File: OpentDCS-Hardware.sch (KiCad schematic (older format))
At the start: 4 parts

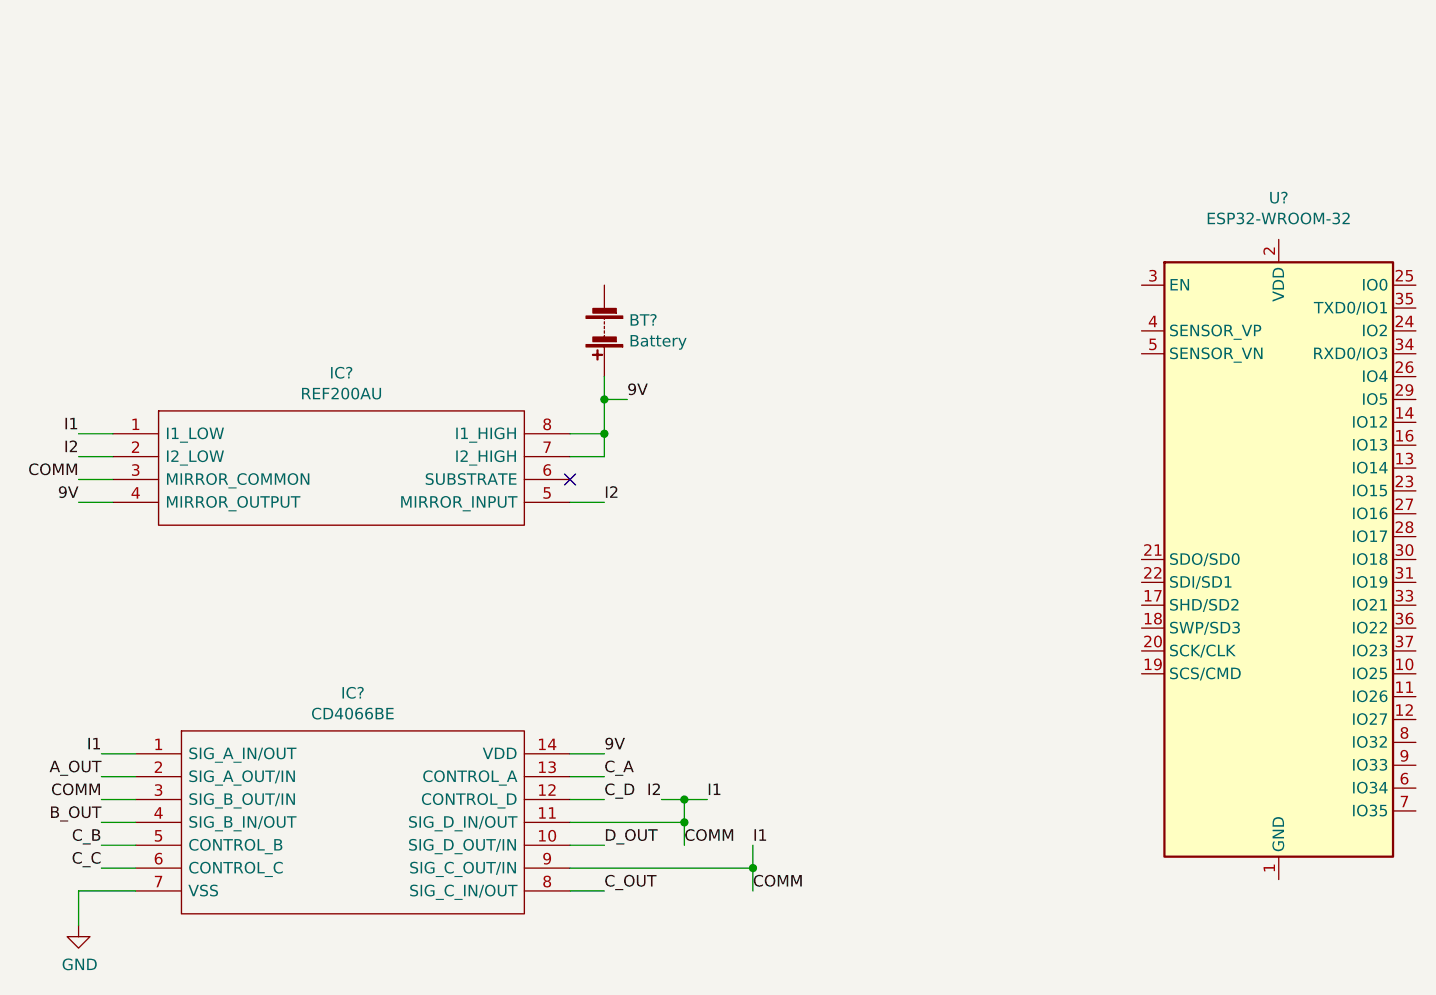
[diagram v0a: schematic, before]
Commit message: Combinações de corrente para o REF200
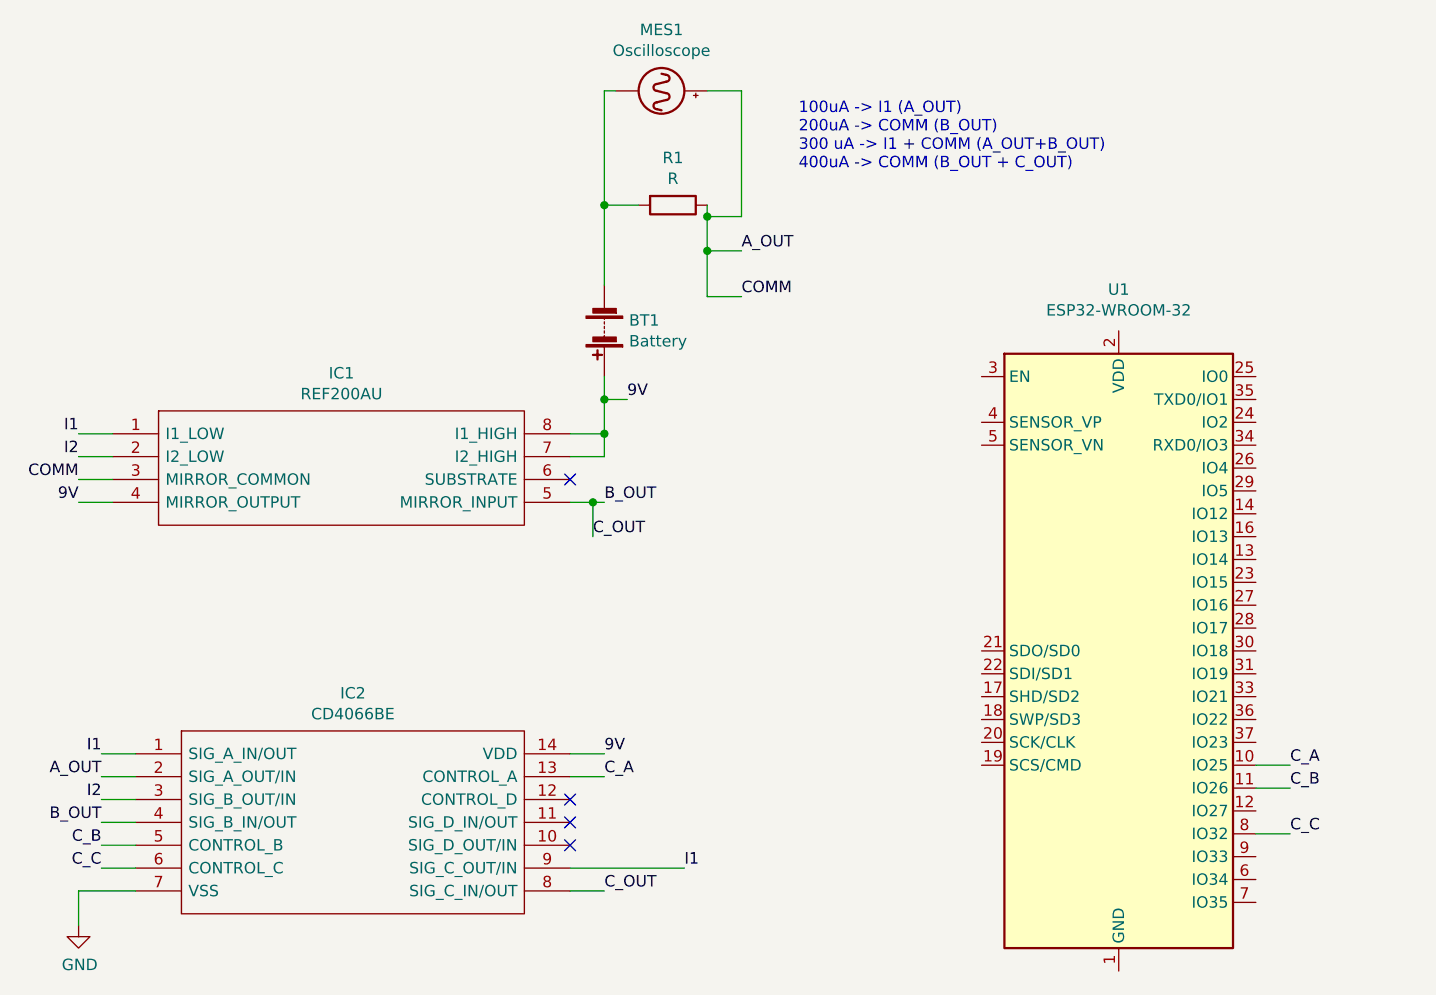
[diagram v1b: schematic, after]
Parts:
- added MES1: Oscilloscope, symbol Device:Oscilloscope
- added R1: R, symbol Device:R
- gave numbers to parts that had none: 4
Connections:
- net C_OUT is gone; now on net B_OUT: IC2.8 (SIG_C_IN/OUT)
- net A_OUT: now also IC1.3 (MIRROR_COMMON), MES1.2 (+), R1.1
- net B_OUT: now also IC1.5 (MIRROR_INPUT)
- net C_A: now also U1.10 (IO25)
- net C_B: now also U1.11 (IO26)
- net C_C: now also U1.8 (IO32)
- net at BT1.2 (-): now also MES1.1 (-), R1.2
- removed net COMM: IC1.1 (I1_LOW), IC1.2 (I2_LOW), IC1.3 (MIRROR_COMMON), IC1.5 (MIRROR_INPUT), IC2.1 (SIG_A_IN/OUT), IC2.11 (SIG_D_IN/OUT), IC2.3 (SIG_B_OUT/IN), IC2.9 (SIG_C_OUT/IN)
- net C_D: no longer names the net of IC2.12 (CONTROL_D)
- net D_OUT: no longer names the net of IC2.10 (SIG_D_OUT/IN)
- new net I1: IC1.1 (I1_LOW), IC2.1 (SIG_A_IN/OUT), IC2.9 (SIG_C_OUT/IN)
- new net I2: IC1.2 (I2_LOW), IC2.3 (SIG_B_OUT/IN)
- no-connect marks 1 -> 4
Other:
- note added: "100uA -> I1 (A_OUT)\n200uA -> COMM (B_OUT)\n300 uA -> I1 + COMM (A_OUT+B_OUT)\n400uA -> COMM (B_OUT + C_OUT)"
- moved on the sheet: U1
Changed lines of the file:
@@
 $EndDescr
 $Comp
-L REF200AU:REF200AU IC?
+L REF200AU:REF200AU IC1
 U 1 1 630E11F9
 P 3200 3350
-F 0 "IC?" H 4200 3615 50  0000 C CNN
+F 0 "IC1" H 4200 3615 50  0000 C CNN
 F 1 "REF200AU" H 4200 3524 50  0000 C CNN
 F 2 "SOIC127P600X175-8N" H 5050 3450 50  0001 L CNN
@@
 $EndComp
 $Comp
-L CD4066BE:CD4066BE IC?
+L CD4066BE:CD4066BE IC2
 U 1 1 630E206E
 P 3300 4750
-F 0 "IC?" H 4250 5015 50  0000 C CNN
+F 0 "IC2" H 4250 5015 50  0000 C CNN
 F 1 "CD4066BE" H 4250 4924 50  0000 C CNN
 F 2 "DIP794W53P254L1930H508Q14N" H 5050 4850 50  0001 L CNN
@@
 $EndComp
 $Comp
-L Device:Battery BT?
+L Device:Battery BT1
 U 1 1 630E301A
 P 5350 2900
-F 0 "BT?" H 5242 2854 50  0000 R CNN
+F 0 "BT1" H 5242 2854 50  0000 R CNN
 F 1 "Battery" H 5242 2945 50  0000 R CNN
 F 2 "" V 5350 2960 50  0001 C CNN
@@
 	3050 3350 3200 3350
 NoConn ~ 5200 3550
-Text Label 5350 3650 0    50   ~ 0
-I2
-Wire Wire Line
-	5200 3650 5350 3650
 Text Label 3150 4750 2    50   ~ 0
 I1
@@
 Text Label 3150 4850 2    50   ~ 0
 A_OUT
-Text Label 3150 4950 2    50   ~ 0
-COMM
 Text Label 3150 5050 2    50   ~ 0
 B_OUT
@@
 C_C
 $Comp
-L power:GND #PWR?
+L power:GND #PWR01
 U 1 1 630E6AF1
 P 3050 5500
-F 0 "#PWR?" H 3050 5250 50  0001 C CNN
+F 0 "#PWR01" H 3050 5250 50  0001 C CNN
 F 1 "GND" H 3055 5327 50  0000 C CNN
 F 2 "" H 3050 5500 50  0001 C CNN
@@
 Text Label 5350 4850 0    50   ~ 0
 C_A
-Text Label 5350 4950 0    50   ~ 0
-C_D
-Text Label 5800 4950 0    50   ~ 0
-I1
-Text Label 5700 5150 0    50   ~ 0
-COMM
-Wire Wire Line
-	5200 5050 5700 5050
-Wire Wire Line
-	5700 5050 5700 4950
-Wire Wire Line
-	5700 5150 5700 5050
-Connection ~ 5700 5050
-Text Label 5350 5150 0    50   ~ 0
-D_OUT
-Wire Wire Line
-	5200 5150 5350 5150
-Text Label 5600 4950 2    50   ~ 0
-I2
-Wire Wire Line
-	5600 4950 5700 4950
-Wire Wire Line
-	5800 4950 5700 4950
-Connection ~ 5700 4950
 Text Label 5350 5350 0    50   ~ 0
 C_OUT
 Wire Wire Line
 	5200 5350 5350 5350
-Text Label 6000 5350 0    50   ~ 0
+Wire Wire Line
+	5200 4850 5350 4850
+Wire Wire Line
+	5200 4750 5350 4750
+Wire Wire Line
+	3150 4850 3300 4850
+Wire Wire Line
+	3150 4950 3300 4950
+Wire Wire Line
+	3150 5050 3300 5050
+Wire Wire Line
+	3150 5150 3300 5150
+Wire Wire Line
+	3150 5250 3300 5250
+$Comp
+L RF_Module:ESP32-WROOM-32 U1
+U 1 1 630EAD24
+P 7600 4300
+F 0 "U1" H 7600 5881 50  0000 C CNN
+F 1 "ESP32-WROOM-32" H 7600 5790 50  0000 C CNN
+F 2 "RF_Module:ESP32-WROOM-32" H 7600 2800 50  0001 C CNN
+F 3 "https://www.espressif.com/sites/default/files/documentation/esp32-wroom-32_datasheet_en.pdf" H 7300 4350 50  0001 C CNN
+	1    7600 4300
+	1    0    0    -1
+$EndComp
+Text Label 8350 4900 0    50   ~ 0
+C_B
+Text Label 8350 4800 0    50   ~ 0
+C_A
+Text Label 8350 5100 0    50   ~ 0
+C_C
+Wire Wire Line
+	8200 4800 8350 4800
+Wire Wire Line
+	8200 4900 8350 4900
+Wire Wire Line
+	8200 5100 8350 5100
+$Comp
+L Device:R R1
+U 1 1 630E6CA4
+P 5650 2350
+F 0 "R1" V 5443 2350 50  0000 C CNN
+F 1 "R" V 5534 2350 50  0000 C CNN
+F 2 "" V 5580 2350 50  0001 C CNN
+F 3 "~" H 5650 2350 50  0001 C CNN
+	1    5650 2350
+	0    1    1    0
+$EndComp
+Text Label 5950 2550 0    50   ~ 0
+A_OUT
+Wire Wire Line
+	5800 2350 5800 2400
+Wire Wire Line
+	5950 2550 5800 2550
+Connection ~ 5800 2550
+Wire Wire Line
+	5800 2550 5800 2750
+Wire Wire Line
+	5950 2750 5800 2750
+Wire Wire Line
+	5350 2700 5350 2350
+Wire Wire Line
+	5350 2350 5500 2350
+$Comp
+L Device:Oscilloscope MES1
+U 1 1 630EA6D5
+P 5600 1850
+F 0 "MES1" V 5333 1850 50  0000 C CNN
+F 1 "Oscilloscope" V 5424 1850 50  0000 C CNN
+F 2 "" V 5600 1950 50  0001 C CNN
+F 3 "~" V 5600 1950 50  0001 C CNN
+	1    5600 1850
+	0    1    1    0
+$EndComp
+Wire Wire Line
+	5400 1850 5350 1850
+Wire Wire Line
+	5350 1850 5350 2350
+Connection ~ 5350 2350
+Wire Wire Line
+	5800 1850 5950 1850
+Wire Wire Line
+	5950 1850 5950 2400
+Wire Wire Line
+	5950 2400 5800 2400
+Connection ~ 5800 2400
+Wire Wire Line
+	5800 2400 5800 2550
+Wire Wire Line
+	5300 3650 5300 3800
+Wire Wire Line
+	5200 3650 5300 3650
+Connection ~ 5300 3650
+Wire Wire Line
+	5300 3650 5350 3650
+Text Notes 6200 2200 0    50   ~ 0
+100uA -> I1 (A_OUT)\n200uA -> COMM (B_OUT)\n300 uA -> I1 + COMM (A_OUT+B_OUT)\n400uA -> COMM (B_OUT + C_OUT)
+Text Label 3150 4950 2    50   ~ 0
+I2
+Text Label 5950 2750 0    50   ~ 0
 COMM
-Text Label 6000 5150 0    50   ~ 0
+Text Label 5350 3650 0    50   ~ 0
+B_OUT
+Text Label 5300 3800 0    50   ~ 0
+C_OUT
+Text Label 5700 5250 0    50   ~ 0
 I1
 Wire Wire Line
-	6000 5350 6000 5250
-Wire Wire Line
-	5200 5250 6000 5250
-Connection ~ 6000 5250
-Wire Wire Line
-	6000 5250 6000 5150
-Wire Wire Line
-	5350 4950 5200 4950
-Wire Wire Line
-	5200 4850 5350 4850
-Wire Wire Line
-	5200 4750 5350 4750
-Wire Wire Line
-	3150 4850 3300 4850
-Wire Wire Line
-	3150 4950 3300 4950
-Wire Wire Line
-	3150 5050 3300 5050
-Wire Wire Line
-	3150 5150 3300 5150
-Wire Wire Line
-	3150 5250 3300 5250
-$Comp
-L RF_Module:ESP32-WROOM-32 U?
-U 1 1 630EAD24
-P 8300 3900
-F 0 "U?" H 8300 5481 50  0000 C CNN
-F 1 "ESP32-WROOM-32" H 8300 5390 50  0000 C CNN
-F 2 "RF_Module:ESP32-WROOM-32" H 8300 2400 50  0001 C CNN
-F 3 "https://www.espressif.com/sites/default/files/documentation/esp32-wroom-32_datasheet_en.pdf" H 8000 3950 50  0001 C CNN
-	1    8300 3900
-	1    0    0    -1
-$EndComp
+	5200 5250 5700 5250
+NoConn ~ 5200 5050
+NoConn ~ 5200 5150
+NoConn ~ 5200 4950
 $EndSCHEMATC
